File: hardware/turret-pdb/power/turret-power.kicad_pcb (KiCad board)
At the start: 2 copper layers, 100 x 95 mm, 29 parts, among them J1 Battery in, J10 Vision 5V, J11 Servo bus 7.5V, J2 12V bench, J3 Arm switch, J4 Pusher, J5 ESC left, J6 ESC right, J7 TTLinker, J8 TFmini Plus, J9 Light gate, U1 Freenove ESP32-S3 WROOM, U2 Adafruit 757, U3 MP1584 7.5V, U4 MP1584 6V, U5 MP1584 5V

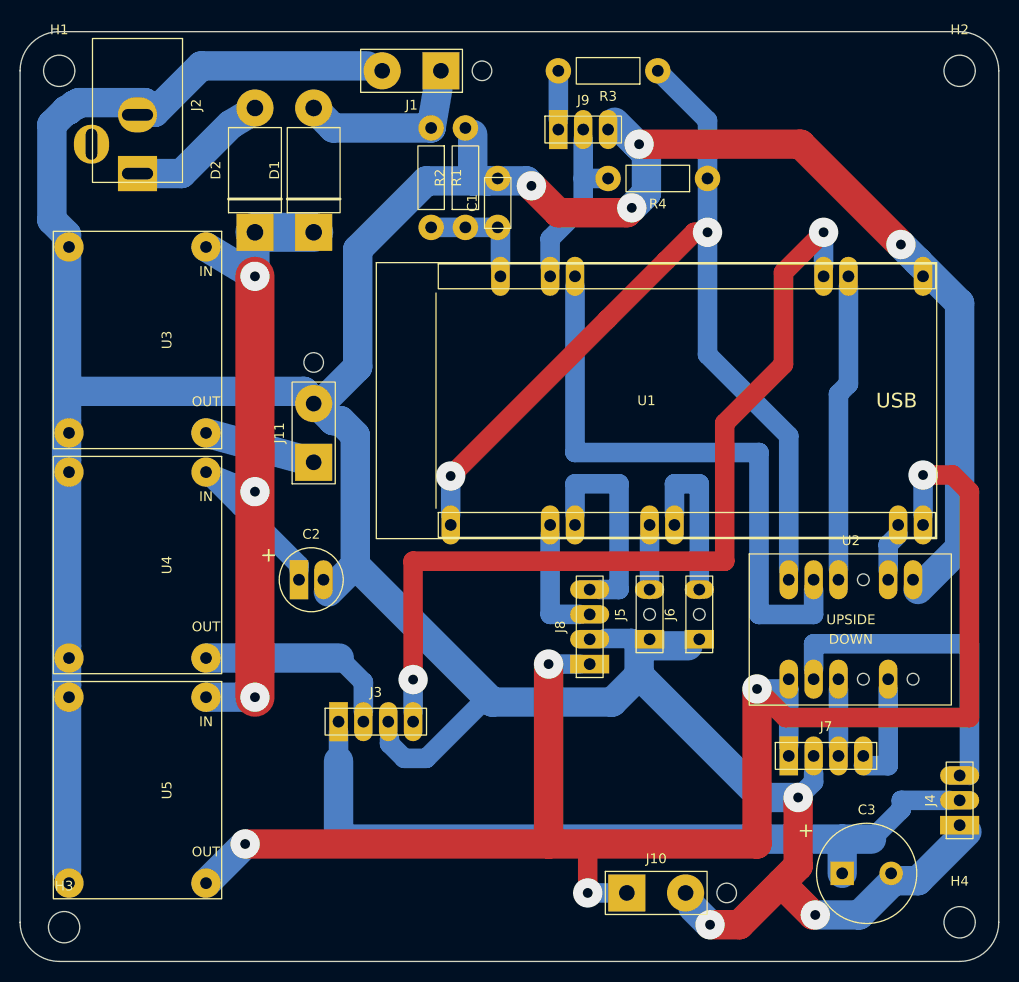
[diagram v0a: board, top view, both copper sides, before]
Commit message: Split the controller board into placed power and logic boards
Co-Authored-By: Claude Opus 5.5 <noreply@anthropic.com>
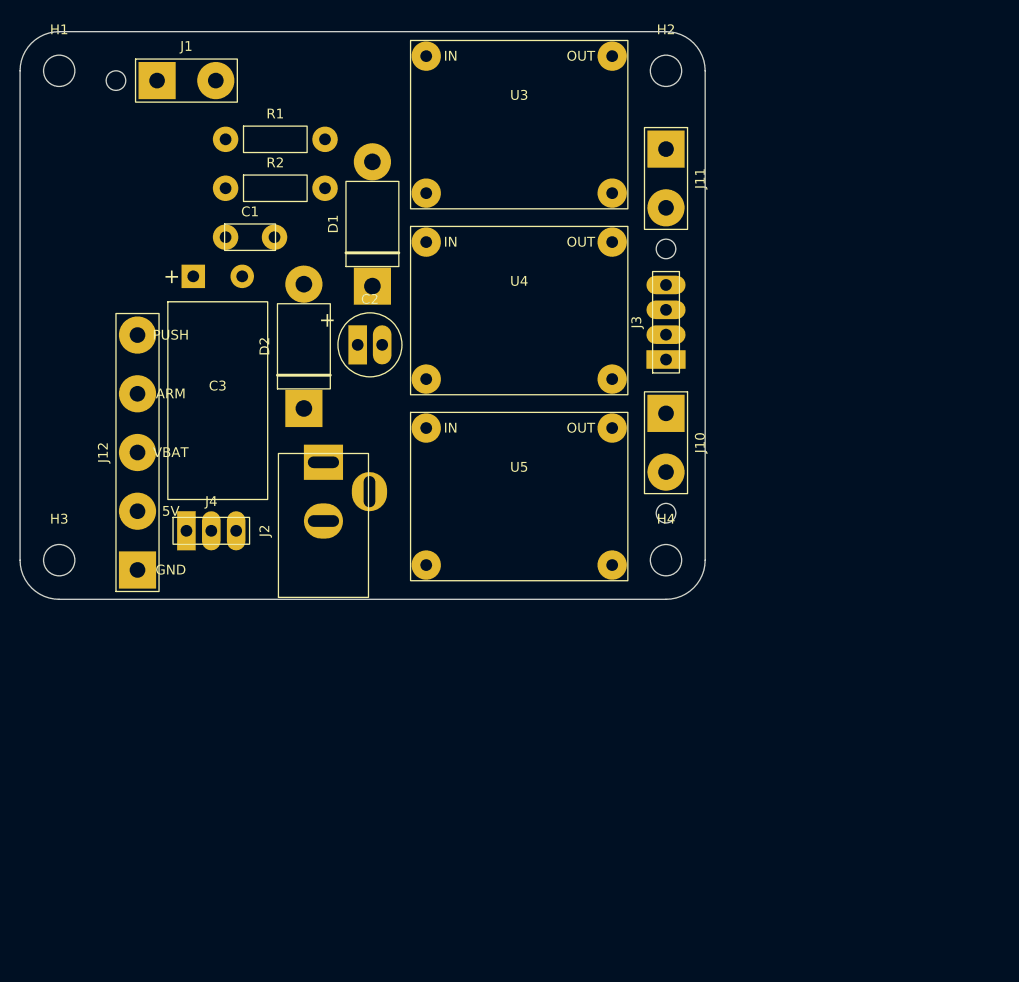
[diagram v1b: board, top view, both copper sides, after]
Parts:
- removed J5: ESC left, turret-power:PinHeader_1x03_P2.54mm_ESC
- removed J6: ESC right, turret-power:PinHeader_1x03_P2.54mm_ESC
- removed J7: TTLinker, turret-power:PinHeader_1x04_P2.54mm
- removed J8: TFmini Plus, turret-power:PinHeader_1x04_P2.54mm
- removed J9: Light gate, turret-power:PinHeader_1x03_P2.54mm
- removed R3: 150, turret-power:R_Axial_P10.16mm_Horizontal
- removed R4: 10k, turret-power:R_Axial_P10.16mm_Horizontal
- removed U1: Freenove ESP32-S3 WROOM, turret-power:Freenove_ESP32-S3_WROOM_Socket
- removed U2: Adafruit 757, turret-power:Adafruit_757_UpsideDown
- added J12: Stack link, turret-power:WirePads_1x05_NoTie, F.Cu at (52.0, 95.0)
- C3: footprint turret-power:CP_Radial_D10.0mm_P5.00mm -> turret-power:CP_Radial_D10.0mm_L20.0mm_P5.00mm_Lying
- J1: footprint turret-power:WirePads_1x02_TieRight -> turret-power:WirePads_1x02_TieLeft
- moved C3 90.1 mm to (57.7, 65.0)
- moved J4 84.5 mm to (57.0, 91.0), turned to 0 degrees
- moved J3 49.9 mm to (106.0, 73.5), turned to 90 degrees
- moved J10 49.2 mm to (106.0, 79.0), turned to 270 degrees
- moved J11 48.2 mm to (106.0, 52.0), turned to 270 degrees
- moved H4 47.6 mm to (106.0, 94.0)
- moved H3 37.5 mm to (44.0, 94.0)
- moved U5 35.5 mm to (81.5, 80.5), turned to 0 degrees
- moved J2 35.1 mm to (71.0, 84.0), turned to 90 degrees
- moved U4 32.5 mm to (81.5, 61.5), turned to 0 degrees
- moved H2 30.0 mm to (106.0, 44.0)
- moved U3 29.8 mm to (81.5, 42.5), turned to 0 degrees
- moved J1 29.0 mm to (54.0, 45.0), turned to 0 degrees
- moved C1 27.8 mm to (61.0, 61.0), turned to 0 degrees
- moved R2 24.8 mm to (61.0, 56.0), turned to 0 degrees
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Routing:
- net GND: track 428.1 -> 0.00 mm, vias 7 -> 0
- net +5V: track 169.0 -> 0.00 mm, vias 5 -> 0
- net +3V3: track 97.1 -> 0.00 mm, vias 2 -> 0
- net ARM_SENSE: track 88.5 -> 0.00 mm, vias 2 -> 0
- net VIN: track 83.7 -> 0.00 mm, vias 3 -> 0
- net PUSH_6V: track 79.1 -> 0.00 mm
- net PUSH_SIG_3V3: track 60.5 -> 0.00 mm
- net PUSH_SIG: track 32.0 -> 0.00 mm
- net BUS_RX_3V3: track 29.4 -> 0.00 mm
- net TF_RX: track 20.5 -> 0.00 mm
- net +6V: track 20.1 -> 0.00 mm
- net VBAT: track 18.8 -> 0.00 mm
- net GATE: track 16.9 -> 0.00 mm
- net ESC_R: track 16.5 -> 0.00 mm
- net VJACK: track 14.7 -> 0.00 mm
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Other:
- board size 100 x 95 mm -> 70 x 58 mm

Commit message: Route the power board
Co-Authored-By: Claude Opus 5.5 <noreply@anthropic.com>
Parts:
- J10: footprint turret-power:WirePads_1x02_TieRight -> turret-power:WirePads_1x02_NoTie
- J3: footprint turret-power:PinHeader_1x04_P2.54mm -> turret-power:WirePads_1x04_NoTie
- moved J1 71.4 mm to (106.0, 94.0), turned to 90 degrees
- moved R1 66.2 mm to (98.5, 105.5), turned to 90 degrees
- moved J11 55.7 mm to (51.0, 43.5), turned to 0 degrees
- moved J3 49.2 mm to (67.0, 43.5), turned to 0 degrees
- moved J10 38.2 mm to (92.0, 43.5), turned to 0 degrees
- moved U3 37.9 mm to (53.0, 67.5), turned to 90 degrees
- moved C3 32.4 mm to (71.0, 94.5), turned to 270 degrees
- moved R2 31.4 mm to (73.0, 85.0), turned to 180 degrees
- moved C1 30.5 mm to (73.0, 89.0), turned to 180 degrees
- moved D1 26.8 mm to (100.0, 78.0), turned to 270 degrees
- moved J12 25.2 mm to (77.1, 97.0)
- moved J2 21.6 mm to (90.0, 94.3)
- moved D2 21.1 mm to (90.0, 77.0), turned to 270 degrees
- moved C2 19.2 mm to (93.5, 75.0)
- moved J4 17.0 mm to (65.0, 76.0)
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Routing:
- net GND: track 0.00 -> 218.7 mm, vias 0 -> 5
- net VIN: track 0.00 -> 82.9 mm, vias 0 -> 3
- net PUSH_6V: track 0.00 -> 75.5 mm, vias 0 -> 3
- net +5V: track 0.00 -> 52.4 mm, vias 0 -> 2
- net ARM_SENSE: track 0.00 -> 35.5 mm
- net VBAT_SENSE: track 0.00 -> 32.5 mm
- net VBAT: track 0.00 -> 16.0 mm
- net PUSH_SIG: track 0.00 -> 5.75 mm
- net +6V: track 0.00 -> 3.50 mm
- net +7V5: track 0.00 -> 2.50 mm
- net VJACK: track 0.00 -> 1.50 mm
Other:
- board size 70 x 58 mm -> 70 x 68 mm

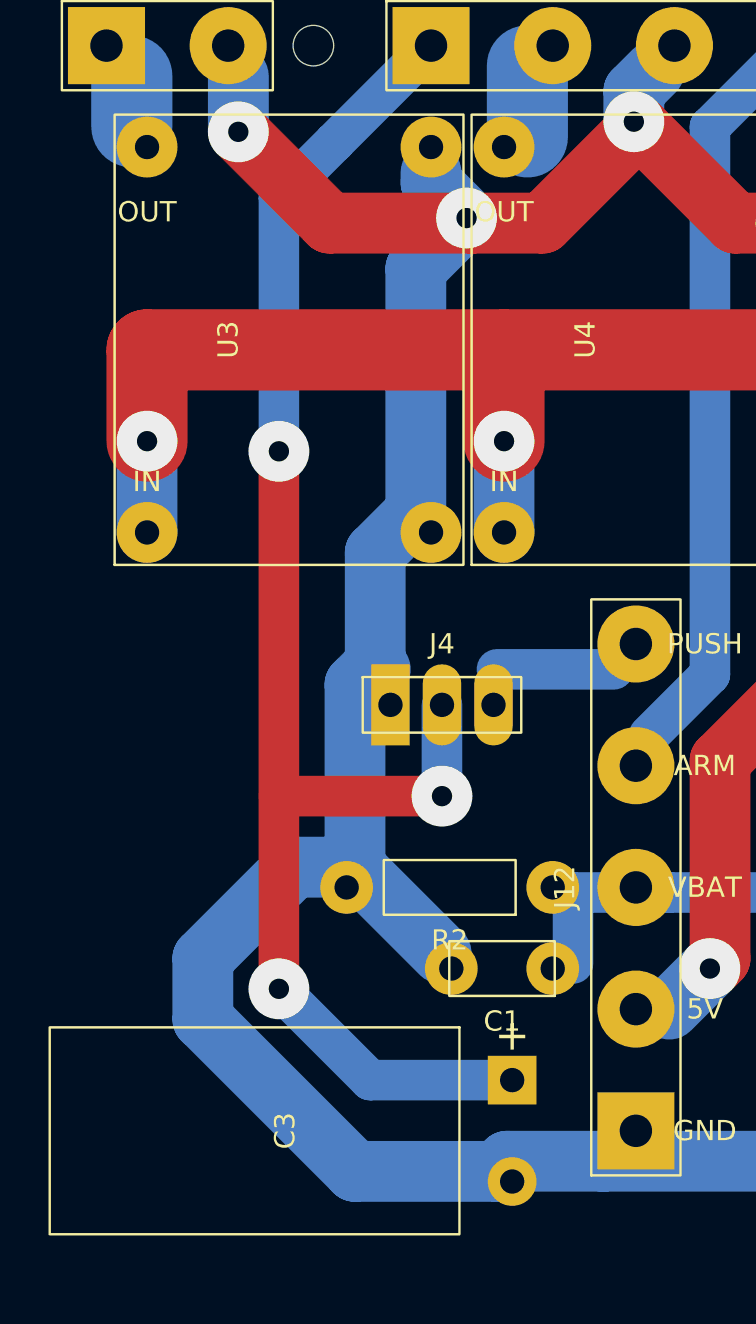
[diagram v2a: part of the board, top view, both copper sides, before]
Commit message: Fix review findings: back-side link soldering, J4 solder holes, 17 mm gap
Co-Authored-By: Claude Opus 5.5 <noreply@anthropic.com>
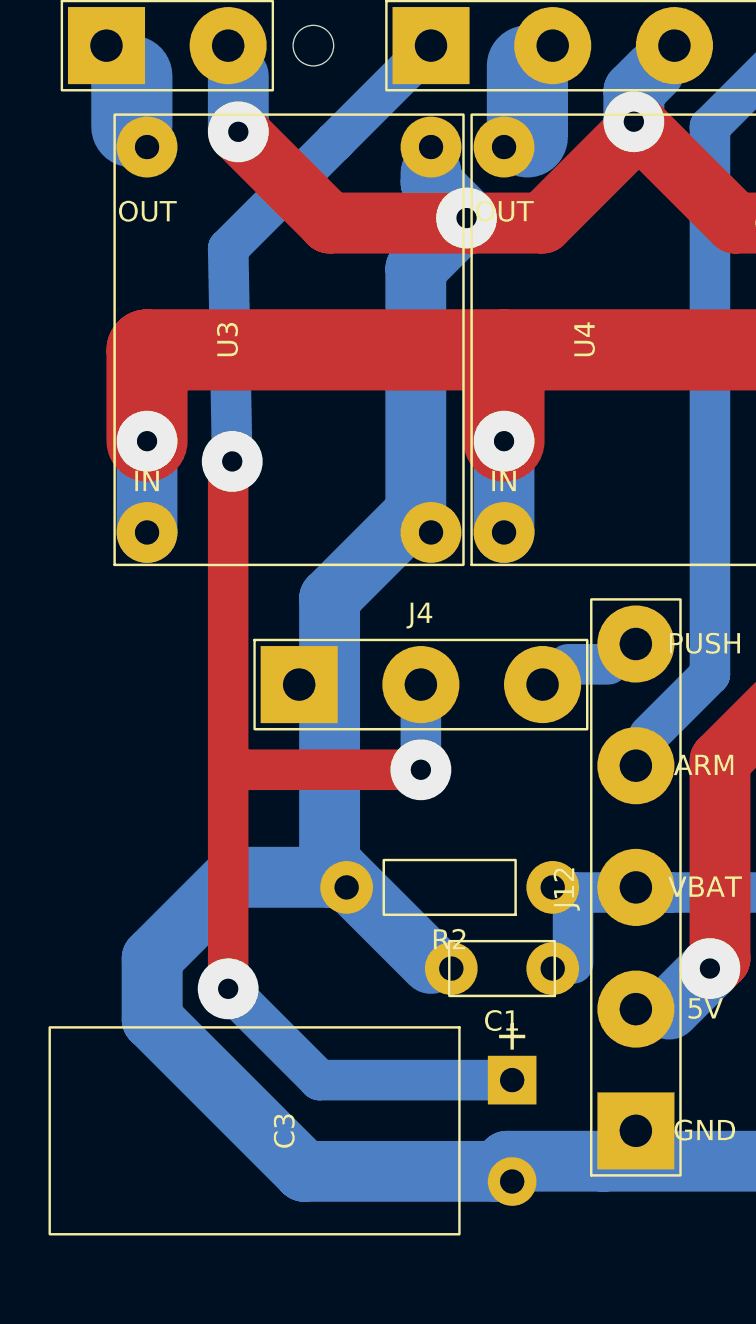
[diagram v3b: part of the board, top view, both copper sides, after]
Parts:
- J4: footprint turret-power:PinHeader_1x03_P2.54mm -> turret-power:WirePads_1x03_NoTie
- moved J4 4.61 mm to (60.5, 75.0)
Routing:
- net GND: track 218.7 -> 223.9 mm
- net PUSH_6V: track 75.5 -> 80.2 mm
- net PUSH_SIG: track 5.75 -> 2.00 mm
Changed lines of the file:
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@@
 		(layer "F.Cu")
 		(at 106 94 90)
-		(descr "Solder holes for stranded wire, zip-tie holes at both ends for strain relief")
+		(descr "Solder holes for stranded wire, zip-tie holes for strain relief")
 		(property "Reference" "J1"
 			(at 3 -3.5 90)
@@
 			)
 		)
-		(property "Description" "Solder holes for stranded wire, zip-tie holes at both ends for strain relief"
+		(property "Description" "Solder holes for stranded wire, zip-tie holes for strain relief"
 			(at 0 0 90)
 			(layer "F.Fab")
@@
 		(fp_rect
 			(start -5.7 -2.7)
-			(end 9.4 2.7)
+			(end 8.4 2.7)
 			(stroke
 				(width 0.05)
@@
 		(layer "F.Cu")
 		(at 51 43.5)
-		(descr "Solder holes for stranded wire, zip-tie holes at both ends for strain relief")
+		(descr "Solder holes for stranded wire, zip-tie holes for strain relief")
 		(property "Reference" "J11"
 			(at 3 -3.5)
@@
 			)
 		)
-		(property "Description" "Solder holes for stranded wire, zip-tie holes at both ends for strain relief"
+		(property "Description" "Solder holes for stranded wire, zip-tie holes for strain relief"
 			(at 0 0)
 			(layer "F.Fab")
@@
 		)
 		(fp_rect
-			(start -3.4 -2.7)
+			(start -2.4 -2.7)
 			(end 11.7 2.7)
 			(stroke
@@
 		(layer "F.Cu")
 		(at 67 43.5)
-		(descr "Solder holes for stranded wire, zip-tie holes at both ends for strain relief")
+		(descr "Solder holes for stranded wire")
 		(property "Reference" "J3"
 			(at 9 -3.5)
@@
 			)
 		)
-		(property "Description" "Solder holes for stranded wire, zip-tie holes at both ends for strain relief"
+		(property "Description" "Solder holes for stranded wire"
 			(at 0 0)
 			(layer "F.Fab")
@@
 		)
 		(fp_rect
-			(start -3.4 -2.7)
-			(end 21.4 2.7)
+			(start -2.4 -2.7)
+			(end 20.4 2.7)
 			(stroke
 				(width 0.05)
@@
 		(embedded_fonts no)
 	)
-	(footprint "turret-power:PinHeader_1x03_P2.54mm"
-		(layer "F.Cu")
-		(at 65 76)
-		(descr "1x3 2.54 mm male header, pads on the solder side only")
+	(footprint "turret-power:WirePads_1x03_NoTie"
+		(layer "F.Cu")
+		(at 60.5 75)
+		(descr "Solder holes for stranded wire")
 		(property "Reference" "J4"
-			(at 2.54 -3)
+			(at 6 -3.5)
 			(layer "F.SilkS")
 			(effects
@@
 		)
 		(property "Value" "Pusher"
-			(at 2.54 3)
+			(at 6 3.5)
 			(layer "F.Fab")
 			(effects
@@
 			)
 		)
-		(property "Description" "1x3 2.54 mm male header, pads on the solder side only"
+		(property "Description" "Solder holes for stranded wire"
 			(at 0 0)
 			(layer "F.Fab")
@@
 		(duplicate_pad_numbers_are_jumpers no)
 		(fp_rect
-			(start -1.27 -1.27)
-			(end 6.35 1.27)
-			(stroke
-				(width 0.1)
-				(type solid)
-			)
-			(fill no)
-			(layer "F.Fab")
-		)
-		(fp_rect
-			(start -1.37 -1.37)
-			(end 6.45 1.37)
+			(start -2.2 -2.2)
+			(end 14.2 2.2)
 			(stroke
 				(width 0.12)
@@
 		)
 		(fp_rect
-			(start -1.77 -1.77)
-			(end 6.85 1.77)
+			(start -2.4 -2.7)
+			(end 14.4 2.7)
 			(stroke
 				(width 0.05)
@@
 		(pad "1" thru_hole rect
 			(at 0 0)
-			(size 1.9 4)
-			(drill 1.2)
-			(layers "*.Cu" "B.Mask")
-			(zone_connect 0)
+			(size 3.8 3.8)
+			(drill 1.6)
+			(layers "*.Cu" "*.Mask")
 			(net "GND")
 		)
-		(pad "2" thru_hole oval
-			(at 2.54 0)
-			(size 1.9 4)
-			(drill 1.2)
-			(layers "*.Cu" "B.Mask")
-			(zone_connect 0)
+		(pad "2" thru_hole circle
+			(at 6 0)
+			(size 3.8 3.8)
+			(drill 1.6)
+			(layers "*.Cu" "*.Mask")
 			(net "PUSH_6V")
 		)
-		(pad "3" thru_hole oval
-			(at 5.08 0)
-			(size 1.9 4)
-			(drill 1.2)
-			(layers "*.Cu" "B.Mask")
-			(zone_connect 0)
+		(pad "3" thru_hole circle
+			(at 12 0)
+			(size 3.8 3.8)
+			(drill 1.6)
+			(layers "*.Cu" "*.Mask")
 			(net "PUSH_SIG")
 		)
 		(embedded_fonts no)
-		(model "${KICAD10_3DMODEL_DIR}/Connector_PinHeader_2.54mm.3dshapes/PinHeader_1x03_P2.54mm_Vertical.step"
-			(offset
-				(xyz 0 0 0)
-			)
-			(scale
-				(xyz 1 1 1)
-			)
-			(rotate
-				(xyz 0 0 -90)
-			)
-		)
 	)
 	(footprint "turret-power:CP_Radial_D10.0mm_L20.0mm_P5.00mm_Lying"
@@
 		(layer "F.Cu")
 		(at 92 43.5)
-		(descr "Solder holes for stranded wire, zip-tie holes at both ends for strain relief")
+		(descr "Solder holes for stranded wire")
 		(property "Reference" "J10"
 			(at 3 -3.5)
@@
 			)
 		)
-		(property "Description" "Solder holes for stranded wire, zip-tie holes at both ends for strain relief"
+		(property "Description" "Solder holes for stranded wire"
 			(at 0 0)
 			(layer "F.Fab")
@@
 		)
 		(fp_rect
-			(start -3.4 -2.7)
-			(end 9.4 2.7)
+			(start -2.4 -2.7)
+			(end 8.4 2.7)
 			(stroke
 				(width 0.05)
@@
 		(layer "F.Cu")
 		(at 77.1 97 90)
-		(descr "Solder holes for stranded wire, zip-tie holes at both ends for strain relief")
+		(descr "Solder holes for stranded wire")
 		(property "Reference" "J12"
 			(at 12 -3.5 90)
@@
 			)
 		)
-		(property "Description" "Solder holes for stranded wire, zip-tie holes at both ends for strain relief"
+		(property "Description" "Solder holes for stranded wire"
 			(at 0 0 90)
 			(layer "F.Fab")
@@
 		)
 		(fp_rect
-			(start -3.4 -2.7)
-			(end 27.4 2.7)
+			(start -2.4 -2.7)
+			(end 26.4 2.7)
 			(stroke
 				(width 0.05)
@@
 	(segment
 		(start 62.25 48.25)
-		(end 59.5 51)
+		(end 57 53.5)
 		(width 2)
 		(layer "B.Cu")
@@
 	)
 	(segment
-		(start 59.5 51)
-		(end 59.5 63.5)
+		(start 57 53.5)
+		(end 57.2 64)
 		(width 2)
 		(layer "B.Cu")
@@
 	)
 	(segment
-		(start 59.5 63.5)
-		(end 59.5 90)
+		(start 57.2 64)
+		(end 57 65)
 		(width 2)
 		(layer "F.Cu")
@@
 	)
 	(segment
-		(start 59.5 80.5)
-		(end 67.54 80.5)
+		(start 57 65)
+		(end 57 90)
 		(width 2)
 		(layer "F.Cu")
@@
 	)
 	(segment
-		(start 67.54 80.5)
-		(end 67.54 76)
+		(start 57 79.2)
+		(end 66.5 79.2)
 		(width 2)
-		(layer "B.Cu")
+		(layer "F.Cu")
 		(net "PUSH_6V")
 	)
 	(segment
-		(start 59.5 90)
-		(end 64 94.5)
+		(start 66.5 79.2)
+		(end 66.5 75)
 		(width 2)
 		(layer "B.Cu")
@@
 	)
 	(segment
-		(start 64 94.5)
+		(start 57 90)
+		(end 61.5 94.5)
+		(width 2)
+		(layer "B.Cu")
+		(net "PUSH_6V")
+	)
+	(segment
+		(start 61.5 94.5)
 		(end 71 94.5)
 		(width 2)
@@
 	)
 	(segment
-		(start 70.25 74.25)
-		(end 76 74.25)
+		(start 73.75 74)
+		(end 75.75 74)
 		(width 2)
 		(layer "B.Cu")
@@
 	(segment
 		(start 66.25 66.5)
-		(end 64.25 68.5)
-		(width 3)
-		(layer "B.Cu")
-		(net "GND")
-	)
-	(segment
-		(start 64.25 68.5)
-		(end 64.25 74)
-		(width 3)
-		(layer "B.Cu")
-		(net "GND")
-	)
-	(segment
-		(start 64.25 74)
-		(end 64.5 74.25)
-		(width 3)
-		(layer "B.Cu")
-		(net "GND")
-	)
-	(segment
-		(start 64.25 74)
-		(end 63.25 75)
-		(width 3)
-		(layer "B.Cu")
-		(net "GND")
-	)
-	(segment
-		(start 63.25 75)
-		(end 63.25 84)
-		(width 3)
-		(layer "B.Cu")
-		(net "GND")
-	)
-	(segment
-		(start 63.25 84)
-		(end 67.5 88.25)
+		(end 62 70.75)
+		(width 3)
+		(layer "B.Cu")
+		(net "GND")
+	)
+	(segment
+		(start 62 70.75)
+		(end 62 73.5)
+		(width 3)
+		(layer "B.Cu")
+		(net "GND")
+	)
+	(segment
+		(start 62 73.5)
+		(end 62 84.5)
+		(width 3)
+		(layer "B.Cu")
+		(net "GND")
+	)
+	(segment
+		(start 62 83.75)
+		(end 67 88.75)
 		(width 3)
 		(layer "B.Cu")
@@
 	)
 	(segment
-		(start 63.25 84)
-		(end 60.25 84)
-		(width 3)
-		(layer "B.Cu")
-		(net "GND")
-	)
-	(segment
-		(start 60.25 84)
-		(end 55.75 88.5)
-		(width 3)
-		(layer "B.Cu")
-		(net "GND")
-	)
-	(segment
-		(start 55.75 88.5)
-		(end 55.75 91.5)
-		(width 3)
-		(layer "B.Cu")
-		(net "GND")
-	)
-	(segment
-		(start 55.75 91.5)
-		(end 63.25 99)
-		(width 3)
-		(layer "B.Cu")
-		(net "GND")
-	)
-	(segment
-		(start 63.25 99)
+		(start 62 84.5)
+		(end 57.25 84.5)
+		(width 3)
+		(layer "B.Cu")
+		(net "GND")
+	)
+	(segment
+		(start 57.25 84.5)
+		(end 53.25 88.5)
+		(width 3)
+		(layer "B.Cu")
+		(net "GND")
+	)
+	(segment
+		(start 53.25 88.5)
+		(end 53.25 91.5)
+		(width 3)
+		(layer "B.Cu")
+		(net "GND")
+	)
+	(segment
+		(start 53.25 91.5)
+		(end 60.75 99)
+		(width 3)
+		(layer "B.Cu")
+		(net "GND")
+	)
+	(segment
+		(start 60.75 99)
 		(end 70.25 99)
 		(width 3)
@@
 	)
 	(via
-		(at 59.5 63.5)
+		(at 57.2 64)
 		(size 3)
 		(drill 1)
@@
 	)
 	(via
-		(at 67.54 80.5)
+		(at 66.5 79.2)
 		(size 3)
 		(drill 1)
@@
 	)
 	(via
-		(at 59.5 90)
+		(at 57 90)
 		(size 3)
 		(drill 1)
